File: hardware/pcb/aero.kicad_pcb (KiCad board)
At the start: 4 copper layers, 41 x 50 mm, 218 parts, among them CON1 USB-MICRO-B, CON2 MMCX_CONN, J1 CORTEX_DBG_CONN, J2 LiPoly_Conn, P1 CONN_01X03, Q1 BSS138, SW1 SW_PUSH, U1 STM32L151C8, U10 BU4SU69G2, U11 BU4SU69G2, U12 NC7WZ17, U13 u-blox_max-7c/q, U14 NC7WZ17, U2 nRF8001, U3 2450BM14A0002, U4 ms5611, U5 BMX055, U6 AT45DB321E, U7 BQ24040DSQ, U8 TPS783, U9 TPS61041, Y1 Crystal, Y2 32.768KHz, Y3 16MHz

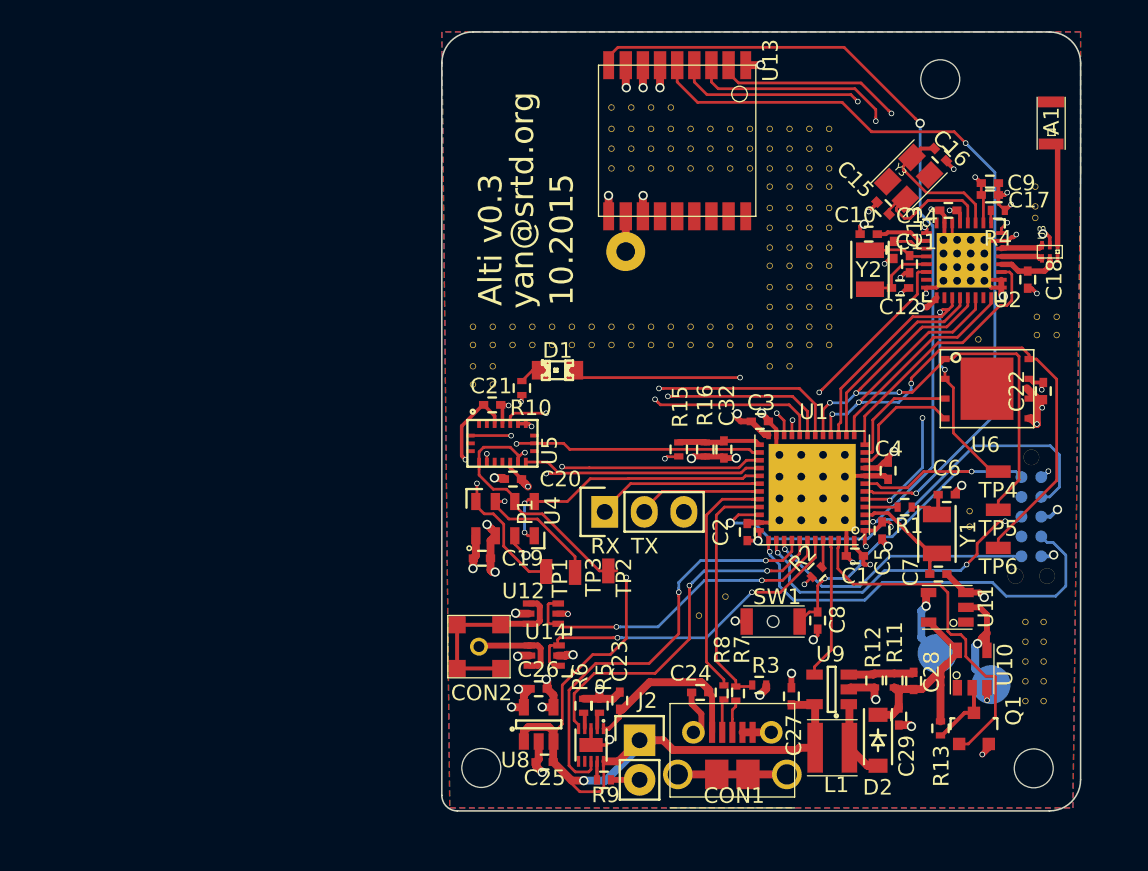
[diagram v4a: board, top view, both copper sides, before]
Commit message: now with normal vias
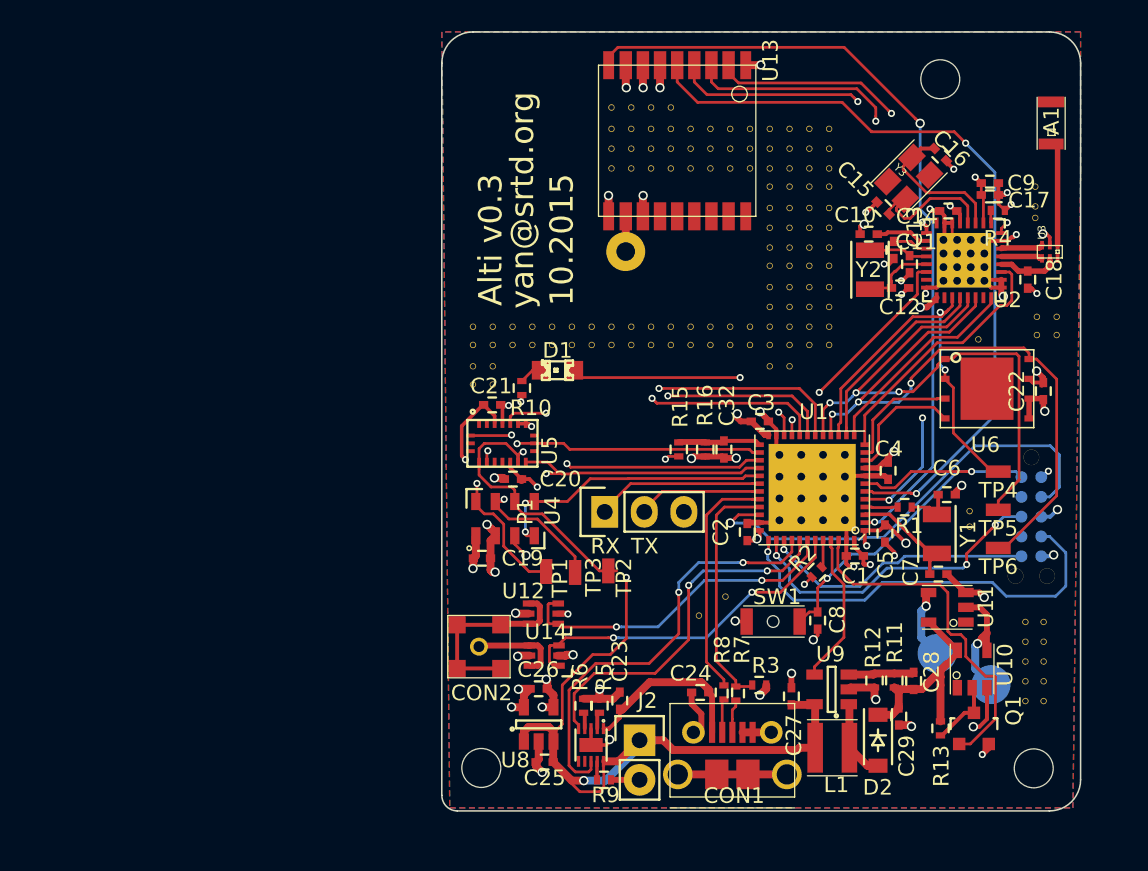
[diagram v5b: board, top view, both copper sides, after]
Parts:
- moved C5 0.27 mm to (153.4, 97.2)
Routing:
- net GND: track 104.0 -> 109.1 mm, vias 48 -> 49
- net /warn/PIEZO_EN: track 9.24 -> 9.96 mm
- net /bmx055/MISO: track 33.0 -> 33.7 mm
- net +3V: track 44.4 -> 44.8 mm, vias 25 -> 24
- net Net-(AUD1-Pad2): vias 2 -> 1
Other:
- rule via_min_size: 0.3556 -> 0.4572
